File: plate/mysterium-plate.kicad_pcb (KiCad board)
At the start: 2 copper layers, 347.7 x 119.1 mm, 2 parts

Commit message: Add ISO support
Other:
- outline, holes or cut-outs redrawn

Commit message: Add split backspace support
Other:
- outline, holes or cut-outs redrawn
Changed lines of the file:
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@@
   (general
     (thickness 1.6)
-    (drawings 786)
+    (drawings 785)
     (tracks 0)
     (zones 0)
@@
       (drillshape 0)
       (scaleselection 1)
-      (outputdirectory "plate/Gerber plate/"))
+      (outputdirectory "Gerber plate/"))
   )
   (net 0 "")
@@
     (fp_arc (start -13.8136 0.18) (end -13.925 -3.95) (angle -180) (layer F.Mask) (width 0.5))
   )
+  (gr_line (start 288.432738 123.985408) (end 288.432742 124.205969) (layer Edge.Cuts) (width 0.2))
+  (gr_line (start 319.308738 123.985414) (end 319.308759 124.205969) (layer Edge.Cuts) (width 0.2))
+  (gr_arc (start 319.395738 122.205968) (end 320.395738 122.205968) (angle 62.83851153) (layer Edge.Cuts) (width 0.2))
+  (gr_arc (start 320.308738 123.985414) (end 319.308738 123.985414) (angle 62.83851153) (layer Edge.Cuts) (width 0.2))
+  (gr_arc (start 287.432738 123.985408) (end 288.432738 123.985408) (angle -62.83851153) (layer Edge.Cuts) (width 0.2))
+  (gr_arc (start 288.345738 122.205962) (end 287.345738 122.205962) (angle -62.83851153) (layer Edge.Cuts) (width 0.2))
+  (gr_arc (start 319.395737 110.205962) (end 320.395738 110.205962) (angle -90) (layer Edge.Cuts) (width 0.2))
+  (gr_line (start 320.395738 122.205968) (end 320.395738 110.205962) (layer Edge.Cuts) (width 0.2))
+  (gr_line (start 287.345738 110.205962) (end 287.345738 122.205962) (layer Edge.Cuts) (width 0.2))
+  (gr_arc (start 288.345738 110.205962) (end 288.345738 109.205962) (angle -90) (layer Edge.Cuts) (width 0.2))
   (gr_arc (start 42.17175 181.111347) (end 43.17175 181.111347) (angle -62.83851153) (layer Edge.Cuts) (width 0.2))
   (gr_line (start 51.17175 180.3319) (end 66.04775 180.3319) (layer Edge.Cuts) (width 0.2))
@@
   (gr_line (start 139.708161 167.355992) (end 139.708161 179.355999) (layer Edge.Cuts) (width 0.2))
   (gr_line (start 149.233167 148.305982) (end 149.233167 160.305989) (layer Edge.Cuts) (width 0.2))
-  (gr_arc (start 296.138695 109.205961) (end 296.138695 110.205962) (angle -60) (layer Edge.Cuts) (width 0.2))
   (gr_line (start 231.195711 123.205969) (end 243.195717 123.205969) (layer Edge.Cuts) (width 0.2))
   (gr_arc (start 362.258282 122.205968) (end 362.258282 123.205969) (angle -90) (layer Edge.Cuts) (width 0.2))
@@
   (gr_arc (start 57.458117 198.406009) (end 57.458117 199.40601) (angle -90) (layer Edge.Cuts) (width 0.2))
   (gr_arc (start 350.258275 122.205968) (end 349.258275 122.205968) (angle -90) (layer Edge.Cuts) (width 0.2))
-  (gr_line (start 309.870753 109.205961) (end 297.870747 109.205961) (layer Edge.Cuts) (width 0.2))
+  (gr_line (start 319.390753 109.205961) (end 288.340747 109.205961) (layer Edge.Cuts) (width 0.2))
   (gr_arc (start 302.633249 198.406009) (end 301.633249 198.406009) (angle -90) (layer Edge.Cuts) (width 0.2))
   (gr_arc (start 281.295738 98.393455) (end 281.295738 99.393456) (angle -90) (layer Edge.Cuts) (width 0.2))
@@
   (gr_line (start 211.1457 110.205962) (end 211.1457 122.205968) (layer Edge.Cuts) (width 0.2))
   (gr_arc (start 233.670712 98.393455) (end 233.670712 99.393456) (angle -90) (layer Edge.Cuts) (width 0.2))
-  (gr_arc (start 44.16386 181.356) (end 43.163859 181.356) (angle -90) (layer Edge.Cuts) (width 0.2))
   (gr_line (start 307.395752 99.393456) (end 319.395758 99.393456) (layer Edge.Cuts) (width 0.2))
   (gr_arc (start 255.008224 198.406009) (end 254.008223 198.406009) (angle -90) (layer Edge.Cuts) (width 0.2))
-  (gr_line (start 318.308758 110.205962) (end 311.602805 110.205962) (layer Edge.Cuts) (width 0.2))
   (gr_arc (start 278.820736 141.255978) (end 277.820736 141.255978) (angle -90) (layer Edge.Cuts) (width 0.2))
   (gr_arc (start 90.795635 98.393455) (end 90.795635 99.393456) (angle -90) (layer Edge.Cuts) (width 0.2))
@@
   (gr_line (start 369.308285 142.255979) (end 381.308292 142.255979) (layer Edge.Cuts) (width 0.2))
   (gr_line (start 162.139423 199.40601) (end 186.045686 199.40601) (layer Edge.Cuts) (width 0.2))
-  (gr_arc (start 318.308758 111.205962) (end 319.308758 111.205962) (angle -90) (layer Edge.Cuts) (width 0.2))
   (gr_arc (start 200.333194 160.305989) (end 200.333194 161.305989) (angle -90) (layer Edge.Cuts) (width 0.2))
   (gr_arc (start 71.745625 122.205968) (end 71.745625 123.205969) (angle -90) (layer Edge.Cuts) (width 0.2))
@@
   (gr_line (start 135.945659 123.205969) (end 147.945666 123.205969) (layer Edge.Cuts) (width 0.2))
   (gr_arc (start 78.795628 122.205968) (end 77.795628 122.205968) (angle -90) (layer Edge.Cuts) (width 0.2))
-  (gr_arc (start 309.870753 110.205962) (end 310.736779 109.705961) (angle -60) (layer Edge.Cuts) (width 0.2))
   (gr_line (start 182.570685 129.255972) (end 182.570685 141.255978) (layer Edge.Cuts) (width 0.2))
   (gr_arc (start 78.795628 110.205962) (end 78.795628 109.205961) (angle -90) (layer Edge.Cuts) (width 0.2))
@@
   (gr_line (start 138.420661 128.255971) (end 126.420654 128.255971) (layer Edge.Cuts) (width 0.2))
   (gr_arc (start 233.670712 141.255978) (end 233.670712 142.255979) (angle -90) (layer Edge.Cuts) (width 0.2))
-  (gr_arc (start 311.602805 109.205961) (end 310.736779 109.705961) (angle -60) (layer Edge.Cuts) (width 0.2))
   (gr_line (start 368.308285 186.406003) (end 368.308285 198.406009) (layer Edge.Cuts) (width 0.2))
   (gr_line (start 330.208264 186.406003) (end 330.208264 198.406009) (layer Edge.Cuts) (width 0.2))
@@
   (gr_line (start 239.695715 183.406001) (end 234.695713 183.406001) (layer Edge.Cuts) (width 0.2))
   (gr_arc (start 219.383204 160.305989) (end 219.383204 161.305989) (angle -90) (layer Edge.Cuts) (width 0.2))
-  (gr_line (start 319.308758 124.205969) (end 319.308758 111.205962) (layer Edge.Cuts) (width 0.2))
   (gr_line (start 277.820736 129.255972) (end 277.820736 141.255978) (layer Edge.Cuts) (width 0.2))
   (gr_arc (start 109.845645 98.393455) (end 109.845645 99.393456) (angle -90) (layer Edge.Cuts) (width 0.2))
@@
   (gr_arc (start 343.208271 141.255978) (end 343.208271 142.255979) (angle -90) (layer Edge.Cuts) (width 0.2))
   (gr_line (start 154.99567 123.205969) (end 166.995676 123.205969) (layer Edge.Cuts) (width 0.2))
-  (gr_arc (start 297.870747 110.205962) (end 297.870747 109.205961) (angle -60) (layer Edge.Cuts) (width 0.2))
   (gr_arc (start 186.045686 198.406009) (end 186.045686 199.40601) (angle -90) (layer Edge.Cuts) (width 0.2))
   (gr_arc (start 140.708162 179.355999) (end 139.708161 179.355999) (angle -90) (layer Edge.Cuts) (width 0.2))
@@
   (gr_line (start 262.245728 109.205961) (end 250.245721 109.205961) (layer Edge.Cuts) (width 0.2))
   (gr_arc (start 250.245721 110.205962) (end 250.245721 109.205961) (angle -90) (layer Edge.Cuts) (width 0.2))
-  (gr_line (start 296.138695 110.205962) (end 289.432742 110.205962) (layer Edge.Cuts) (width 0.2))
   (gr_line (start 331.208265 199.40601) (end 343.208271 199.40601) (layer Edge.Cuts) (width 0.2))
-  (gr_arc (start 289.432742 111.205962) (end 289.432742 110.205962) (angle -90) (layer Edge.Cuts) (width 0.2))
-  (gr_line (start 288.432742 111.205962) (end 288.432742 124.205969) (layer Edge.Cuts) (width 0.2))
   (gr_line (start 244.483218 148.305982) (end 244.483218 160.305989) (layer Edge.Cuts) (width 0.2))
   (gr_arc (start 289.432742 124.205969) (end 288.432742 124.205969) (angle -90) (layer Edge.Cuts) (width 0.2))
@@
     (connect_pads (clearance 0.508))
     (min_thickness 0.254)
-    (fill (arc_segments 32) (thermal_gap 0.508) (thermal_bridge_width 0.508))
+    (fill yes (arc_segments 32) (thermal_gap 0.508) (thermal_bridge_width 0.508))
     (polygon
       (pts
@@
     (connect_pads (clearance 0.508))
     (min_thickness 0.254)
-    (fill (arc_segments 32) (thermal_gap 0.508) (thermal_bridge_width 0.508))
+    (fill yes (arc_segments 32) (thermal_gap 0.508) (thermal_bridge_width 0.508))
     (polygon
       (pts
@@
         (xy 304.546 179.832) (xy 288.925 179.832) (xy 287.782 180.721) (xy 287.782 181.737) (xy 281.813 181.737)
         (xy 281.813 167.894) (xy 289.306 167.894) (xy 290.576 166.878) (xy 303.022 166.878)
-      )
-    )
-  )
-  (zone (net 0) (net_name "") (layers F&B.Cu) (hatch edge 0.508)
-    (connect_pads (clearance 0.3))
-    (min_thickness 0.254)
-    (keepout (tracks not_allowed) (vias not_allowed) (copperpour not_allowed))
-    (fill (arc_segments 32) (thermal_gap 0.508) (thermal_bridge_width 0.508))
-    (polygon
-      (pts
-        (xy 311.404 110.744) (xy 318.77 110.744) (xy 318.77 124.587) (xy 312.928 124.587) (xy 312.928 123.698)
-        (xy 311.785 122.682) (xy 296.164 122.682) (xy 295.021 123.571) (xy 295.021 124.587) (xy 289.052 124.587)
-        (xy 289.052 110.744) (xy 296.545 110.744) (xy 297.815 109.728) (xy 310.261 109.728)
       )
     )
@@
       )
     )
+  )
+  (zone (net 0) (net_name "") (layers F&B.Cu) (hatch edge 0.508)
+    (connect_pads (clearance 0.3))
+    (min_thickness 0.254)
+    (keepout (tracks not_allowed) (vias not_allowed) (copperpour not_allowed))
+    (fill (arc_segments 32) (thermal_gap 0.508) (thermal_bridge_width 0.508))
+    (polygon
+      (pts
+        (xy 320.04 122.555) (xy 318.897 123.825) (xy 318.897 124.841) (xy 312.674 124.841) (xy 312.674 123.952)
+        (xy 311.658 122.936) (xy 296.037 122.936) (xy 295.021 123.952) (xy 295.021 124.841) (xy 288.925 124.841)
+        (xy 288.925 123.698) (xy 287.782 122.555) (xy 287.782 109.601) (xy 320.04 109.601)
+      )
+    )

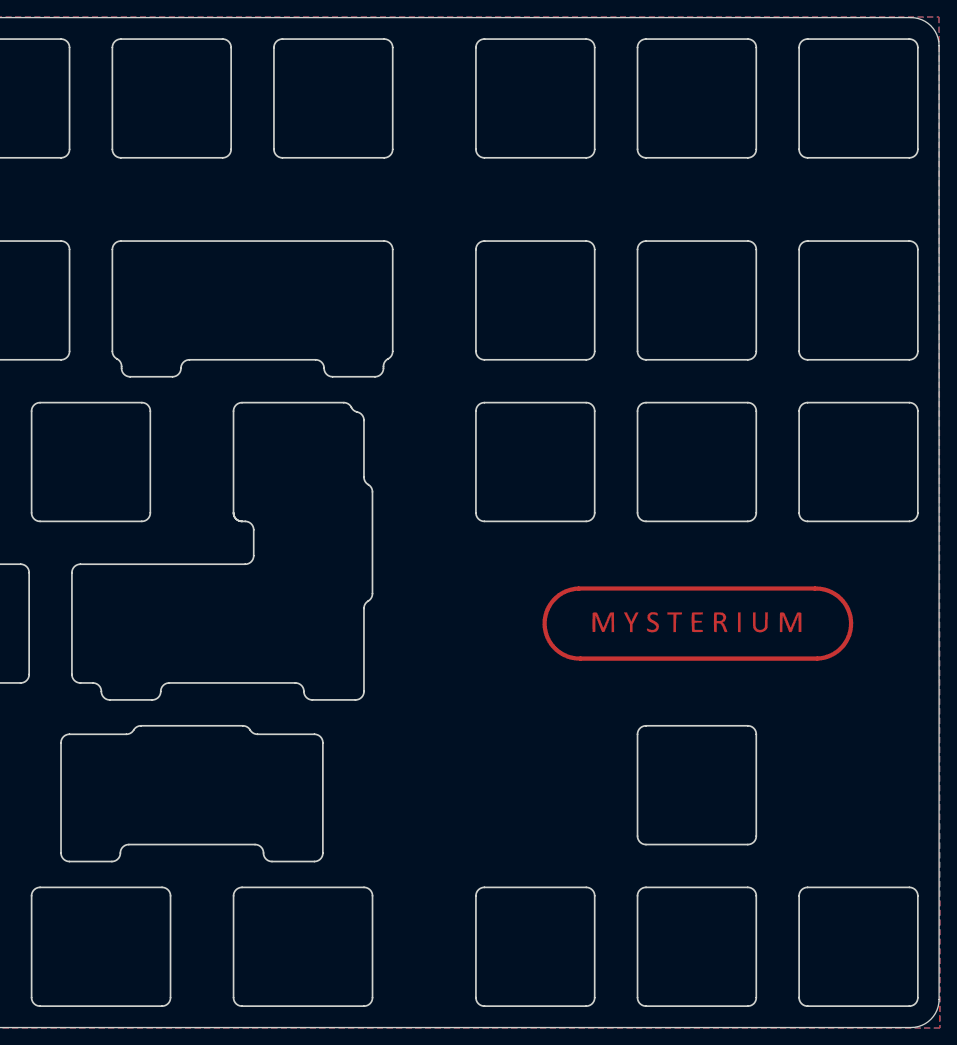
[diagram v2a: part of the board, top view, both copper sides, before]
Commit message: Add support for 0.91" 128x32 OLED display
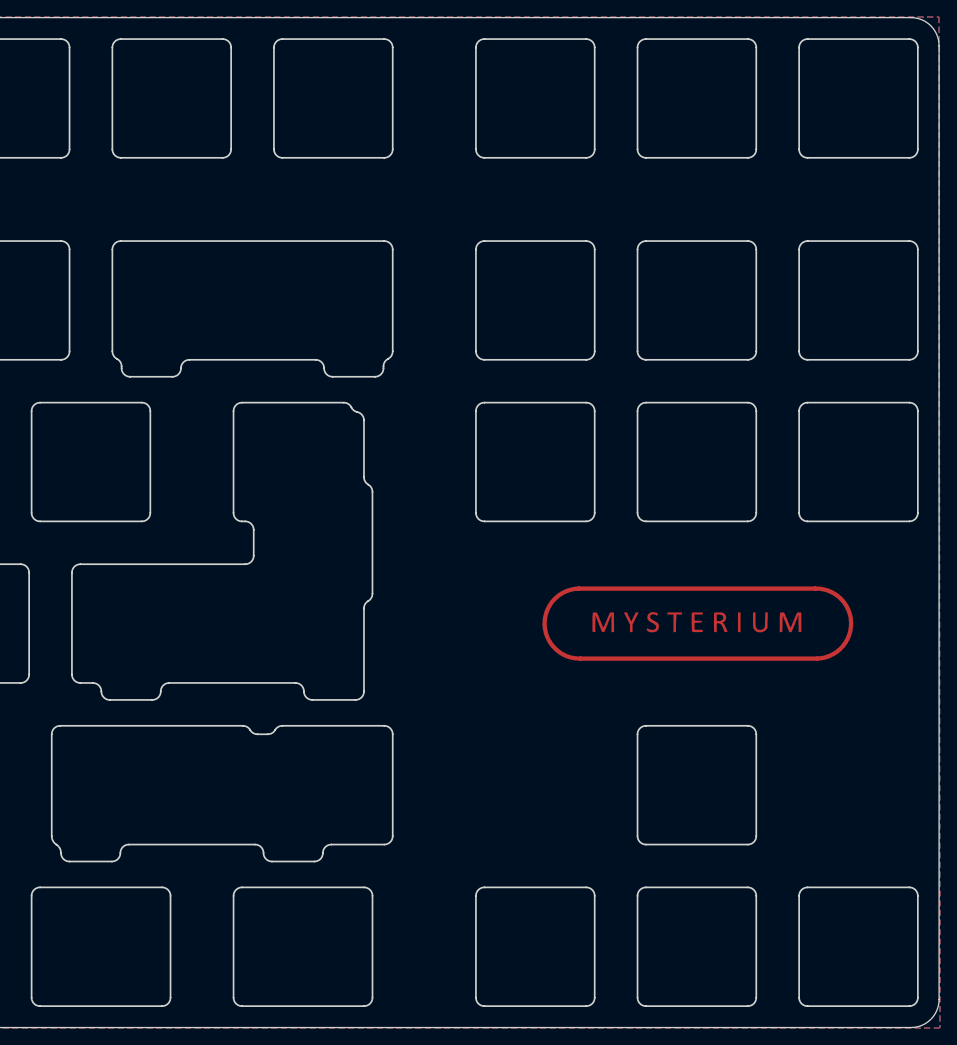
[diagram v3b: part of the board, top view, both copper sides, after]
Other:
- outline, holes or cut-outs redrawn
- board text added: "JLCJLCJLCJLC"

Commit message: Switch to KiCad 6 file formats
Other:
- net class Default removed
